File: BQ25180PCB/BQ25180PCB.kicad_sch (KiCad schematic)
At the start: 7 parts, among them J1 Conn_01x04_Socket, J2 Conn_01x06_Socket, U1 BQ25180

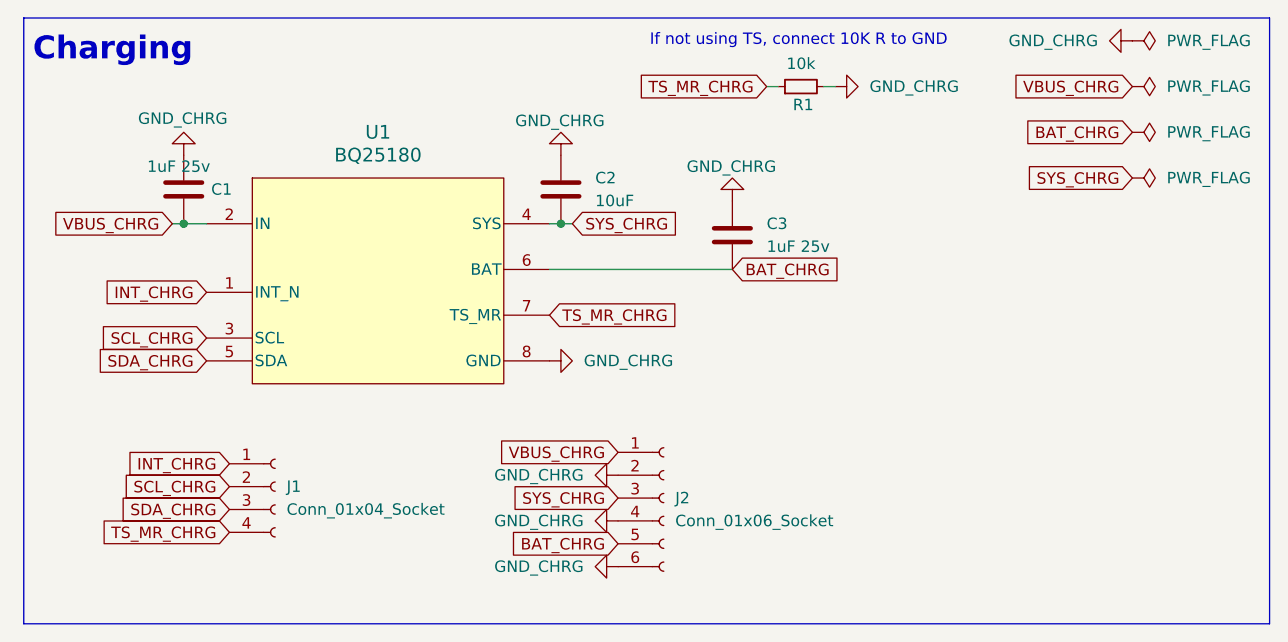
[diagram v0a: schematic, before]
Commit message: bq25180 basic pcb layout
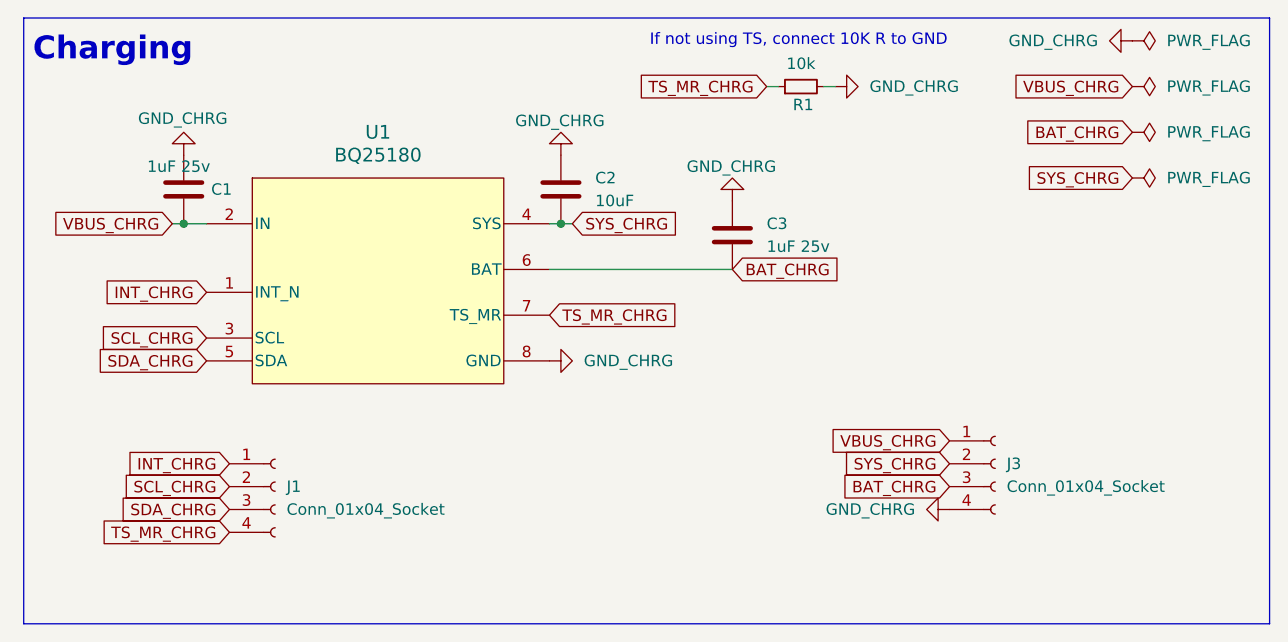
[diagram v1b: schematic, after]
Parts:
- removed J2: Conn_01x06_Socket, Connector_PinSocket_2.54mm:PinSocket_1x06_P2.54mm_Vertical, symbol Connector:Conn_01x06_Socket
- added J3: Conn_01x04_Socket, Connector_PinSocket_2.54mm:PinSocket_1x04_P2.54mm_Vertical, symbol Connector:Conn_01x04_Socket
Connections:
- net BAT_CHRG: now also J3.3 (Pin_3)
- net GND_CHRG: now also J3.4 (Pin_4)
- net SYS_CHRG: now also J3.2 (Pin_2)
- net VBUS_CHRG: now also J3.1 (Pin_1)

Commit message: jlcpcb files
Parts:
- C1, C3: LCSC (none) -> C1712
- C2: LCSC (none) -> C15850
- R1: LCSC (none) -> C17414
- U1: LCSC (none) -> C3682423
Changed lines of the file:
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@@
+			)
+		)
+		(property "LCSC" "C15850"
+			(at 99.06 99.0599 0)
+			(effects
+				(font
+					(size 1.27 1.27)
+				)
+				(hide yes)
 			)
 		)
@@
 			)
 		)
+		(property "LCSC" "C3682423"
+			(at 55.88 104.14 0)
+			(effects
+				(font
+					(size 1.27 1.27)
+				)
+				(hide yes)
+			)
+		)
 		(pin "2"
 		)
@@
 			)
 		)
+		(property "LCSC" "C1712"
+			(at 56.388 100.33 0)
+			(effects
+				(font
+					(size 1.27 1.27)
+				)
+				(hide yes)
+			)
+		)
 		(pin "1"
 		)
@@
 		(property "Description" "Resistor, small symbol"
 			(at 121.92 88.9 0)
+			(effects
+				(font
+					(size 1.27 1.27)
+				)
+				(hide yes)
+			)
+		)
+		(property "LCSC" "C17414"
+			(at 122.174 90.932 0)
 			(effects
 				(font
@@
 			(effects
 				(font
+					(size 1.27 1.27)
+				)
+				(hide yes)
+			)
+		)
+		(property "LCSC" "C1712"
+			(at 118.11 104.1399 0)
+			(effects
+				(font
